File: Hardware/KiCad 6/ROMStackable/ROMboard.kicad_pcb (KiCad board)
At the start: 2 copper layers, 22.9 x 54.6 mm, 10 parts, among them J0 Conn_01x16, J1 Conn_01x16, J2 Conn_01x04, U1 M29F160, U2 74LVC1G19

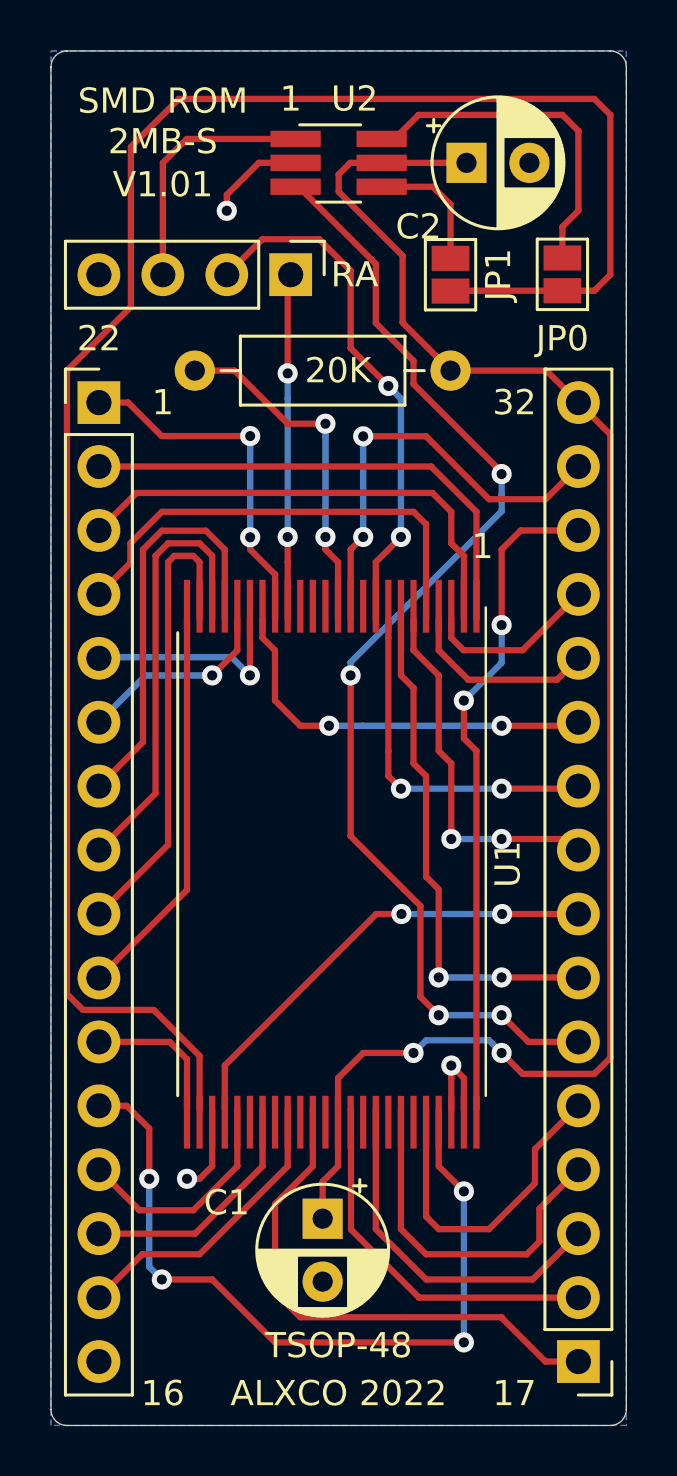
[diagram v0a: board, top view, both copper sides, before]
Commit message: Adjust Orientation of ROMStackable headers
Flip the pin headers to the bottom of the board, to better reflect their actual position when assembled. General cleanup of disconnected traces.
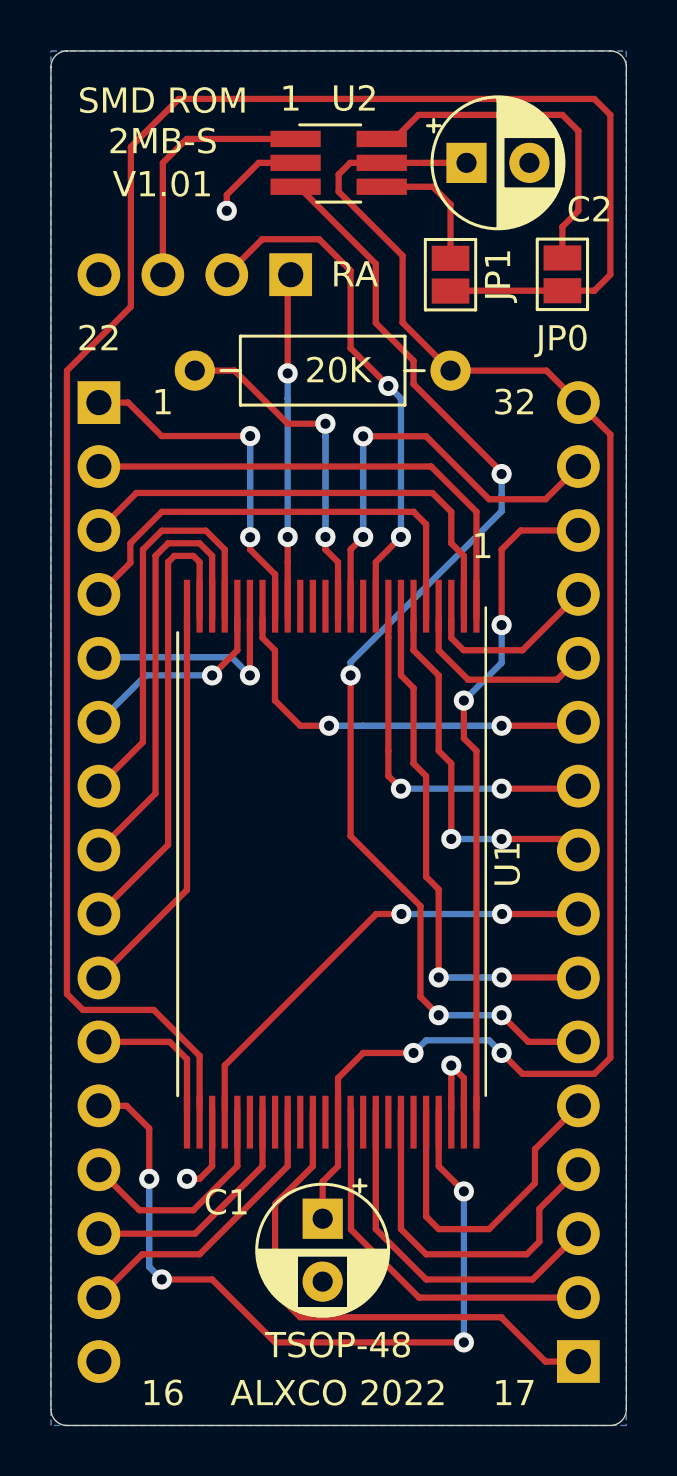
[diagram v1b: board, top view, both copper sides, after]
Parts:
- J0, J1, J2: moved to B.Cu
- turned J0 to 180 degrees
- turned J1 to 0 degrees
- turned J2 to 90 degrees
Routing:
- net /A0: track 32.5 -> 31.3 mm
- net /A8: track 16.5 -> 16.0 mm
